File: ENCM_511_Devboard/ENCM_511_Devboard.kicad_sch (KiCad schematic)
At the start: 9 parts, among them J1 Barrel_Jack_MountingPin, J2 Conn_01x05_Socket, J3 Conn_01x05_Socket, J4 Conn_01x16_Socket, U1 LM1117DT-3.3, U2 PIC24FJ256GA702-I/SO

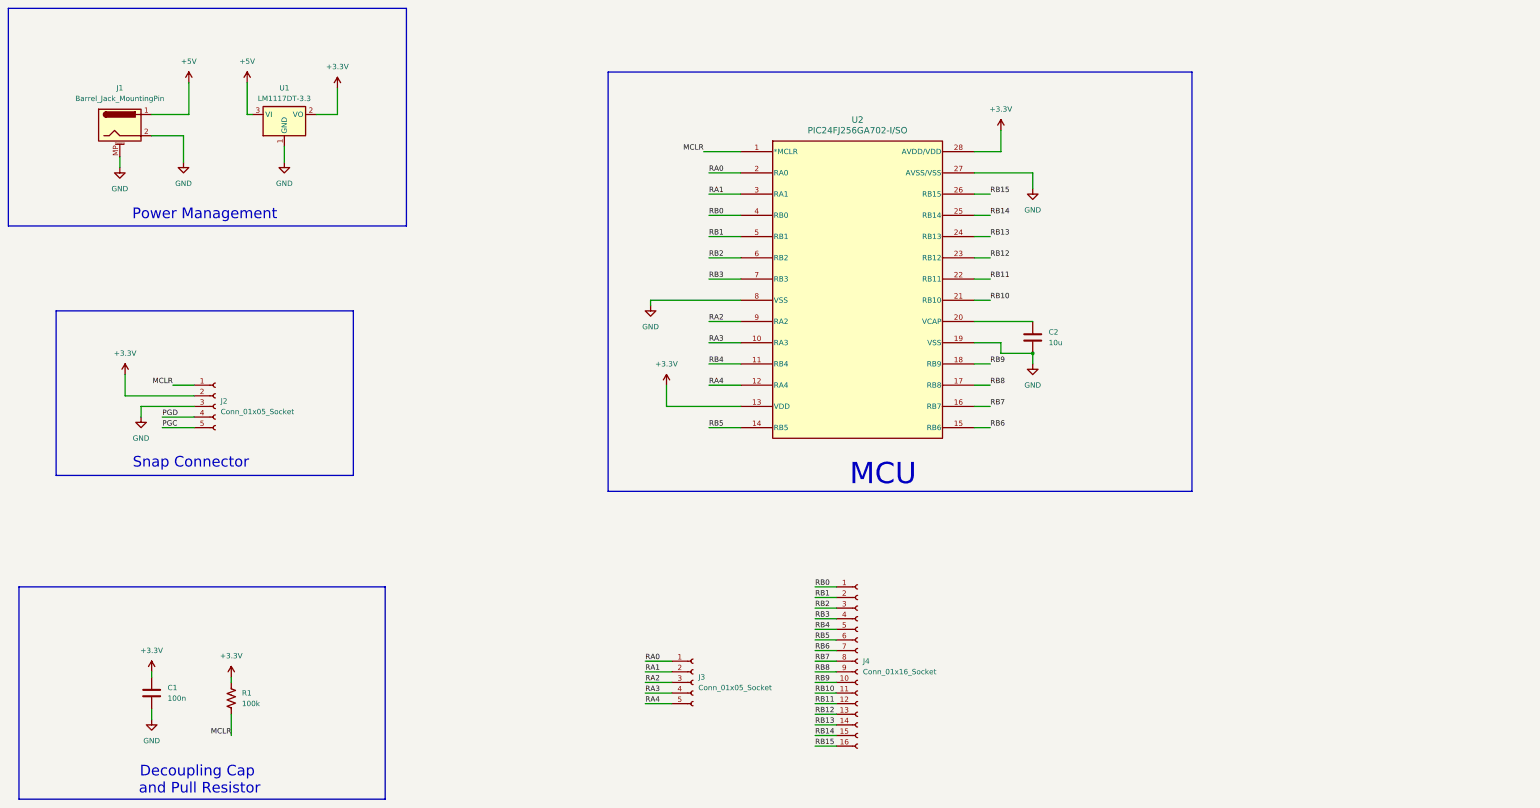
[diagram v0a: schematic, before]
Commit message: Finished Schematic and Began Layout
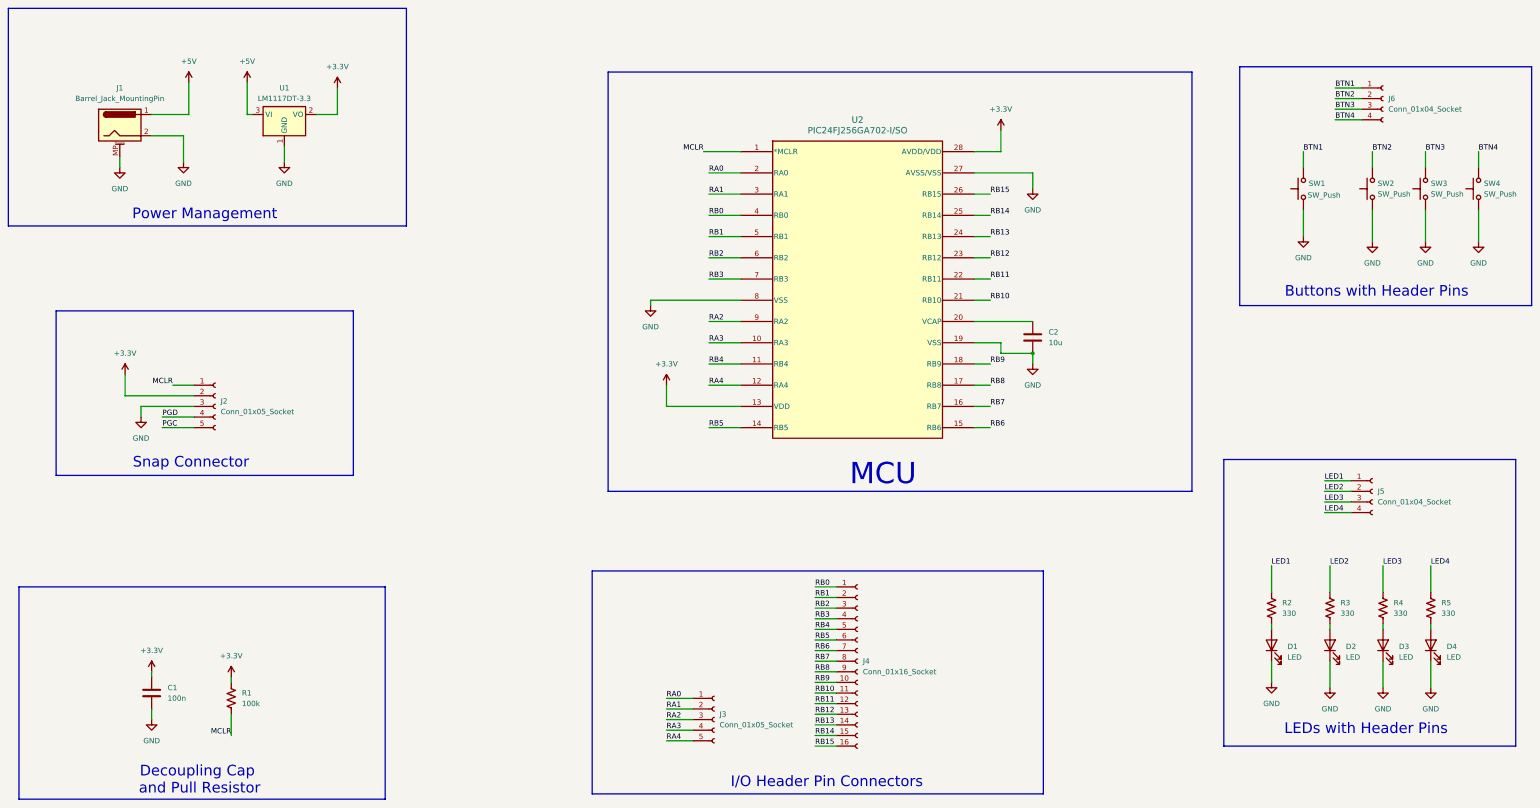
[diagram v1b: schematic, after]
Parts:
- added D1, D2, D3, D4: LED, LED_SMD:LED_1206_3216Metric_Pad1.42x1.75mm_HandSolder, symbol Device:LED
- added J5, J6: Conn_01x04_Socket, Connector_PinSocket_2.54mm:PinSocket_1x04_P2.54mm_Vertical, symbol Connector:Conn_01x04_Socket
- added R2, R3, R4, R5: 330, Resistor_SMD:R_1206_3216Metric_Pad1.30x1.75mm_HandSolder, symbol Device:R_US
- added SW1, SW2, SW3, SW4: SW_Push, Button_Switch_THT:SW_PUSH_6mm, symbol Switch:SW_Push
- C1, C2: footprint (none) -> Capacitor_SMD:C_1206_3216Metric_Pad1.33x1.80mm_HandSolder
- J1: footprint (none) -> 00-footprint-library:BarrelJack_Horizontal_personal
- J2, J3: footprint (none) -> Connector_PinSocket_2.54mm:PinSocket_1x05_P2.54mm_Vertical
- J4: footprint (none) -> Connector_PinSocket_2.54mm:PinSocket_1x16_P2.54mm_Vertical
- R1: footprint (none) -> Resistor_SMD:R_1206_3216Metric_Pad1.30x1.75mm_HandSolder
- U2: footprint SOIC28_SO_MCH -> 00-footprint-library:SOIC28_SO_MCH
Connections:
- net GND: now also D1.1 (K), D2.1 (K), D3.1 (K), D4.1 (K), SW1.1, SW2.1, SW3.1, SW4.1
- new net: D4.2 (A), R5.2
- new net: D3.2 (A), R4.2
- new net: D2.2 (A), R3.2
- new net: D1.2 (A), R2.2
- new net BTN1: J6.1 (Pin_1), SW1.2
- new net BTN2: J6.2 (Pin_2), SW2.2
- new net BTN3: J6.3 (Pin_3), SW3.2
- new net BTN4: J6.4 (Pin_4), SW4.2
- new net LED1: J5.1 (Pin_1), R2.1
- new net LED2: J5.2 (Pin_2), R3.1
- new net LED3: J5.3 (Pin_3), R4.1
- new net LED4: J5.4 (Pin_4), R5.1
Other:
- note added: "Buttons with Header Pins"
- note added: "I/O Header Pin Connectors"
- note added: "LEDs with Header Pins"
- moved on the sheet: J3

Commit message: Fixed an Issue with Debugger Connections
This is for PGD and PGC which were unconnected in the first revision.
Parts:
- added C3: 100n, Capacitor_SMD:C_1206_3216Metric_Pad1.33x1.80mm_HandSolder, symbol Device:C
- added C4: 10 uF, Capacitor_SMD:C_1206_3216Metric_Pad1.33x1.80mm_HandSolder, symbol Device:C_Polarized
- added C5: 10uF, Capacitor_SMD:C_1206_3216Metric_Pad1.33x1.80mm_HandSolder, symbol Device:C_Polarized
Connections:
- net RB0 is gone; now on net PGD/RB0: J4.1 (Pin_1), U2.4 (RB0)
- net RB1 is gone; now on net PGC/RB1: J4.2 (Pin_2), U2.5 (RB1)
- net +3.3V: now also C3.1, C5.1
- net +5V: now also C4.1
- net GND: now also C3.2, C4.2, C5.2
- net PGC renamed PGC/RB1
- net PGD renamed PGD/RB0
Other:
- note added: "Decoupling Cap and Pull Resistor for PIC"
- note removed: "Decoupling Cap and Pull Resistor"
